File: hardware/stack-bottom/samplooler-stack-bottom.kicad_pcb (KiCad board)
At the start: 2 copper layers, 90 x 64 mm, 23 parts, among them J1 To top board, J2 MAX98357A (opt), J3 Qwiic I2C, J4 EXP A, J5 EXP B, SW1 EC11, 25 mm shaft, U1 ESP32-S3_SuperMini, U2 PCM5102A, U4 MPU6050, U5 KY-023

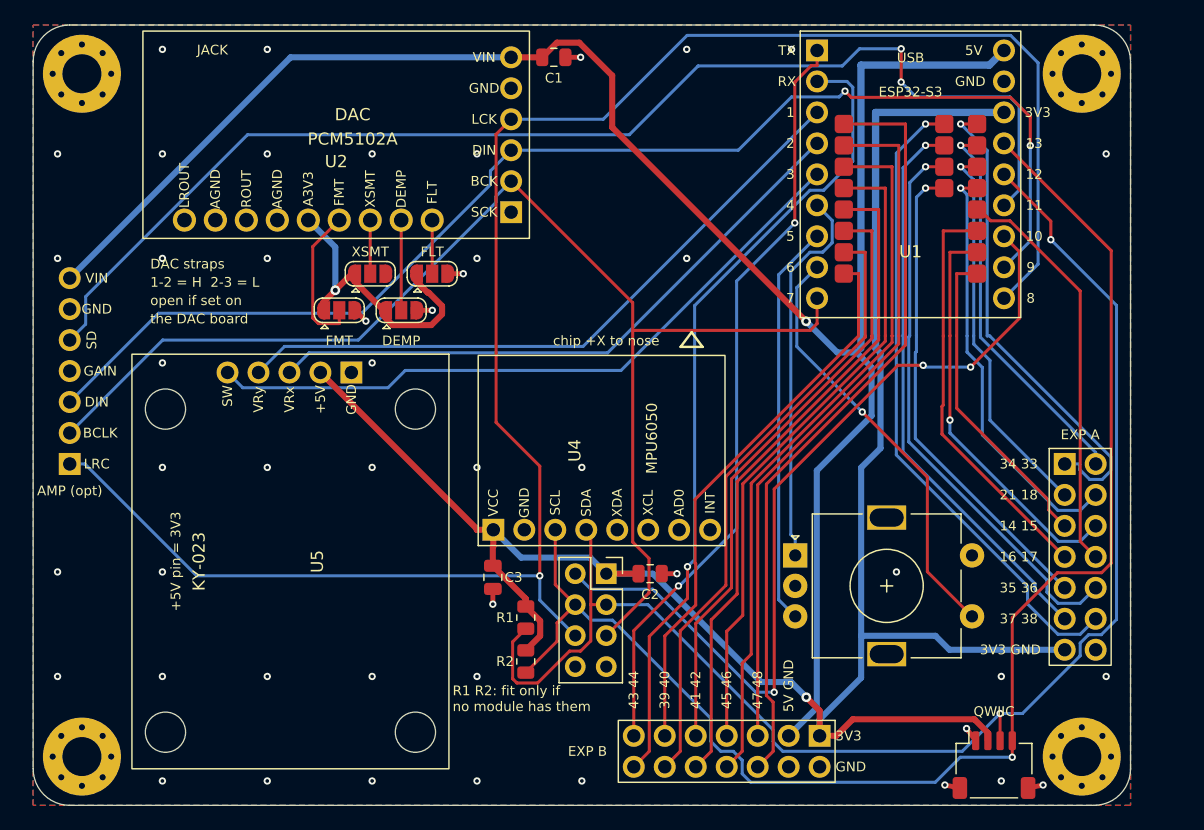
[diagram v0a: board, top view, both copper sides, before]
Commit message: Stack boards at 94 x 46 mm, one-piece JLC panels for the stack and the Mini + Filter
The stack's two boards shrink to 94 x 46 mm with the DAC straps under the
bottom board and both breakout rows in the middle, under the top board.
New hardware/gen/panel.py copies built boards onto one panel with 5 mm
tabs and mouse bites: the stack at 94 x 94 mm (panel-stack/), and the Mini
with the Samplooler Filter at 82 x 94 mm (panel-mini/), with their JLC zips,
BOM and CPL files and renders. kit.py checks router sessions for crossing
tracks of different nets before accepting them. hardware/README.md, CLAUDE.md
and the pcb-design skill describe the panels and the ordering settings.

Co-Authored-By: Claude Fable 5.1 <noreply@anthropic.com>
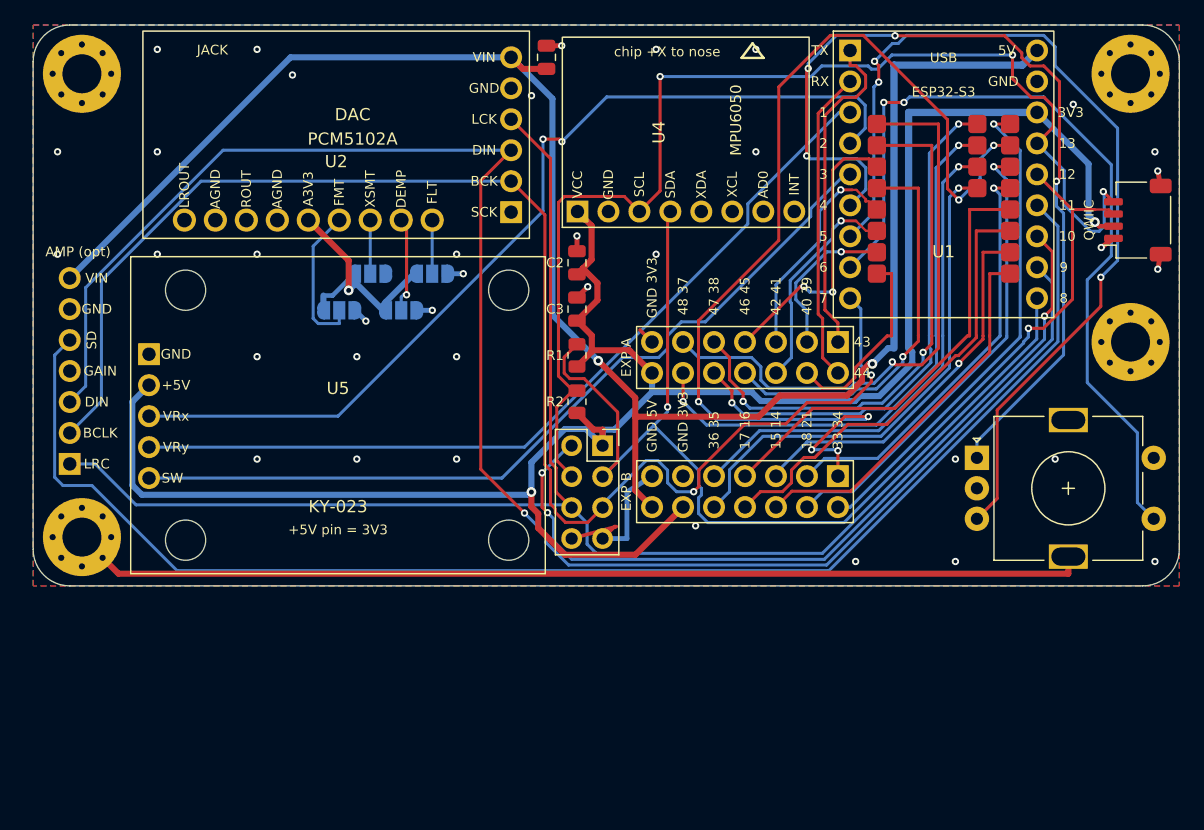
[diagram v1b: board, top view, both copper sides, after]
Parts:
- JP1, JP2, JP3, JP4: moved to B.Cu
- moved J3 46.2 mm to (140.6, 66.0), turned to 90 degrees
- moved H4 34.2 mm to (140.0, 76.0)
- moved U4 27.0 mm to (94.6, 65.3)
- moved C2 26.2 mm to (94.6, 69.5), turned to 90 degrees
- moved C3 23.1 mm to (94.6, 73.3), turned to 90 degrees
- moved R1 21.9 mm to (94.6, 77.1), turned to 90 degrees
- moved R2 21.7 mm to (94.6, 80.9), turned to 90 degrees
- moved J5 21.4 mm to (116.0, 87.0)
- moved J4 21.1 mm to (116.0, 76.0), turned to -90 degrees
- moved H3 18.0 mm to (54.0, 92.0)
- moved SW1 16.9 mm to (127.4, 85.5)
- moved U5 16.7 mm to (59.5, 77.0), turned to 0 degrees
- moved J1 10.5 mm to (96.7, 84.5)
- moved H2 4.00 mm to (140.0, 54.0)
- moved U1 2.71 mm to (117.0, 52.1)
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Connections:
- J4 pad 1: /GPIO34 -> /GPIO43
- J4 pad 10: /GPIO36 -> /GPIO38
- J4 pad 11: /GPIO37 -> /GPIO48
- J4 pad 12: /GPIO38 -> /GPIO37
- J4 pad 13: +3V3 -> GND
- J4 pad 14: GND -> +3V3
- J4 pad 2: /GPIO33 -> /GPIO44
- J4 pad 3: /GPIO21 -> /GPIO40
- J4 pad 4: /GPIO18 -> /GPIO39
- J4 pad 5: /GPIO14 -> /GPIO42
- J4 pad 6: /GPIO15 -> /GPIO41
- J4 pad 7: /GPIO16 -> /GPIO46
- J4 pad 8: /GPIO17 -> /GPIO45
- J4 pad 9: /GPIO35 -> /GPIO47
- J5 pad 1: +3V3 -> /GPIO33
- J5 pad 10: /GPIO42 -> /GPIO35
- J5 pad 11: /GPIO39 -> GND
- J5 pad 12: /GPIO40 -> +3V3
- J5 pad 13: /GPIO43 -> GND
- J5 pad 14: /GPIO44 -> +5V
- J5 pad 2: GND -> /GPIO34
- J5 pad 3: +5V -> /GPIO18
- J5 pad 4: GND -> /GPIO21
- J5 pad 5: /GPIO47 -> /GPIO15
- J5 pad 6: /GPIO48 -> /GPIO14
- J5 pad 7: /GPIO45 -> /GPIO17
- J5 pad 8: /GPIO46 -> /GPIO16
- J5 pad 9: /GPIO41 -> /GPIO36
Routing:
- net GND: track 11.2 -> 109.6 mm, vias 47 -> 37
- net /GPIO33: track 32.1 -> 85.6 mm, vias 1 -> 6
- net /ENC_B: track 33.0 -> 77.2 mm, vias 0 -> 3
- net /ENC_A: track 31.4 -> 74.0 mm, vias 0 -> 4
- net /GPIO44: track 67.0 -> 25.7 mm, vias 1 -> 0
- net /GPIO40: track 50.8 -> 12.9 mm, vias 0 -> 1
- net /I2S_DOUT: track 104.1 -> 141.3 mm, vias 2 -> 1
- net /GPIO42: track 54.8 -> 18.4 mm, vias 0 -> 1
- net /GPIO43: track 62.7 -> 27.2 mm, vias 2 -> 0
- net /GPIO46: track 58.8 -> 23.6 mm, vias 0 -> 2
- net /ENC_SW: track 35.3 -> 67.9 mm, vias 1 -> 2
- net /GPIO41: track 49.7 -> 18.1 mm, vias 0 -> 1
- net /GPIO39: track 45.7 -> 16.0 mm
- net /I2S_WS: track 155.4 -> 127.9 mm, vias 1 -> 0
- net /JOY_X: track 51.1 -> 77.1 mm, vias 0 -> 2
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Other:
- board size 90 x 64 mm -> 94 x 46 mm
- board text added: "43"
- board text added: "44"
- board text added: "R1 R2 (front): fit only if no"
- board text added: "module has I2C pull-ups"
- board text added: "stack bottom rev C 2026-09-28"
- board text removed: "3V3"
- board text removed: "GND"
- board text removed: "R1 R2: fit only if"
- board text removed: "no module has them"
- board text removed: "stack bottom rev B 2026-09-25"

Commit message: Rev D boards, firmware and page changes (work in progress, before the launch cleanup)
Co-Authored-By: Claude Opus 5.5 <noreply@anthropic.com>
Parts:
- removed JP1: FLT, Jumper:SolderJumper-3_P1.3mm_Open_RoundedPad1.0x1.5mm
- removed JP2: DEMP, Jumper:SolderJumper-3_P1.3mm_Open_RoundedPad1.0x1.5mm
- removed JP3: XSMT, Jumper:SolderJumper-3_P1.3mm_Open_RoundedPad1.0x1.5mm
- removed JP4: FMT, Jumper:SolderJumper-3_P1.3mm_Open_RoundedPad1.0x1.5mm
- U5: value KY-023 -> PS2 joystick (KY-023 part); footprint samplooler:KY-023_Joystick -> samplooler:PS2_Joystick
- moved U5 15.9 mm to (75.0, 80.6), turned to 180 degrees
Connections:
- U2 pad 10: /DAC_FMT -> GND
- U2 pad 7: /DAC_FLT -> GND
- U2 pad 8: /DAC_DEMP -> GND
- U2 pad 9: /DAC_XSMT -> /DAC_3V3
- U5 pad 1: GND -> +3V3
- U5 pad 2: +3V3 -> /JOY_X
- U5 pad 3: /JOY_X -> GND
- U5 pad 4: /JOY_Y -> +3V3
- U5 pad 5: /JOY_SW -> /JOY_Y
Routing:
- net /GPIO33: track 85.6 -> 36.9 mm, vias 6 -> 1
- net /ENC_B: track 77.2 -> 31.0 mm, vias 3 -> 2
- net +3V3: track 170.5 -> 130.2 mm, vias 2 -> 1
- net /ENC_A: track 74.0 -> 38.0 mm, vias 4 -> 3
- net /JOY_Y: track 69.8 -> 43.0 mm
- net /GPIO48: track 48.3 -> 26.5 mm, vias 1 -> 2
- net /GPIO47: track 45.0 -> 23.8 mm, vias 2 -> 1
- net /I2S_WS: track 127.9 -> 148.3 mm, vias 0 -> 1
- net /GPIO46: track 23.6 -> 40.9 mm
- net +5V: track 148.1 -> 165.3 mm
- net /I2C_SDA: track 101.3 -> 87.4 mm, vias 2 -> 3
- net /GPIO15: track 31.3 -> 45.2 mm, vias 1 -> 0
- net /I2C_SCL: track 97.5 -> 84.8 mm
- net /DAC_FMT: track 12.4 -> 0.00 mm
- net /DAC_3V3: track 20.8 -> 8.58 mm, vias 1 -> 0
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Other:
- board text added: "DAC: FLT DEMP FMT = L, XSMT = H"
- board text added: "stack bottom rev D 2026-10-15"
- board text removed: "1-2 = H 2-3 = L"
- board text removed: "DAC straps"
- board text removed: "DEMP"
- board text removed: "FLT"
- board text removed: "FMT"
- board text removed: "XSMT"
- board text removed: "open if set on"
- board text removed: "stack bottom rev C 2026-09-28"
- board text removed: "the DAC board"
